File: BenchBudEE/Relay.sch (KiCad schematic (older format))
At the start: 0 parts

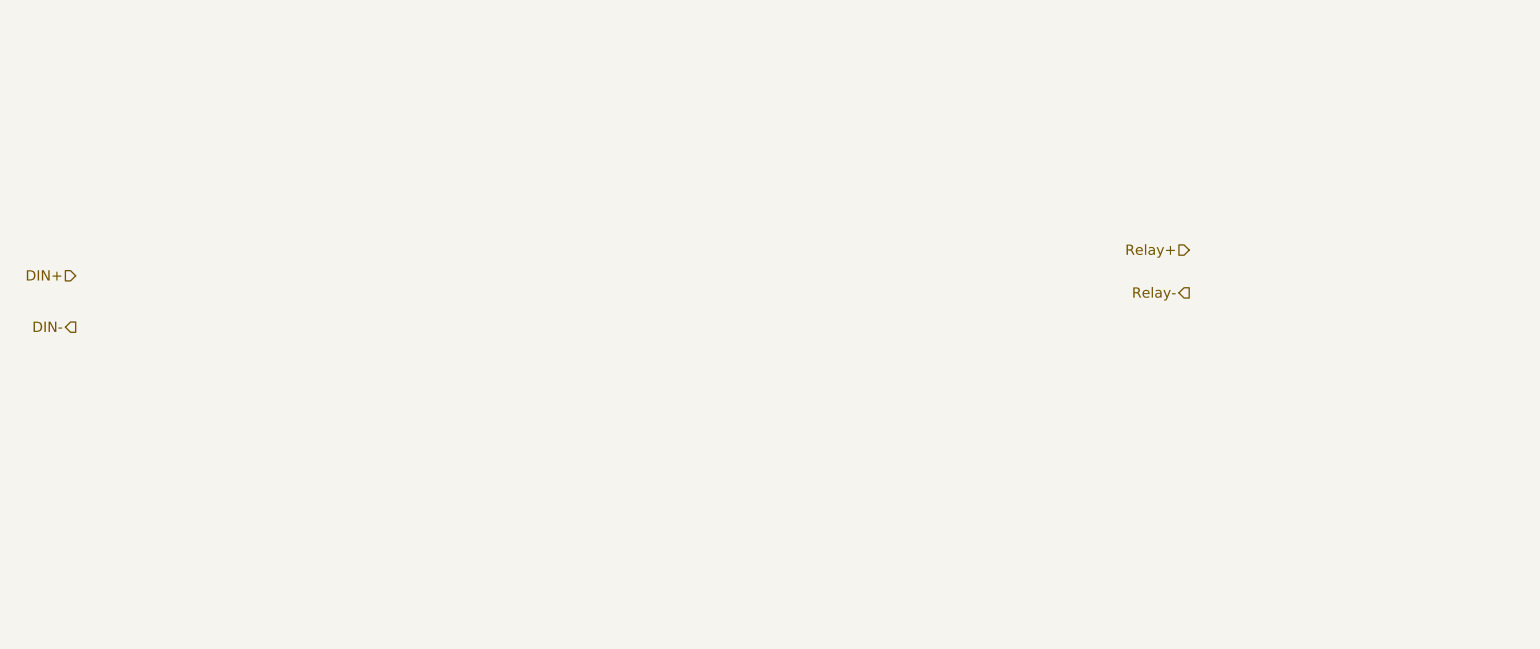
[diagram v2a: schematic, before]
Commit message: Relay block diagram
Relay block diagram and BenchBudEE library created
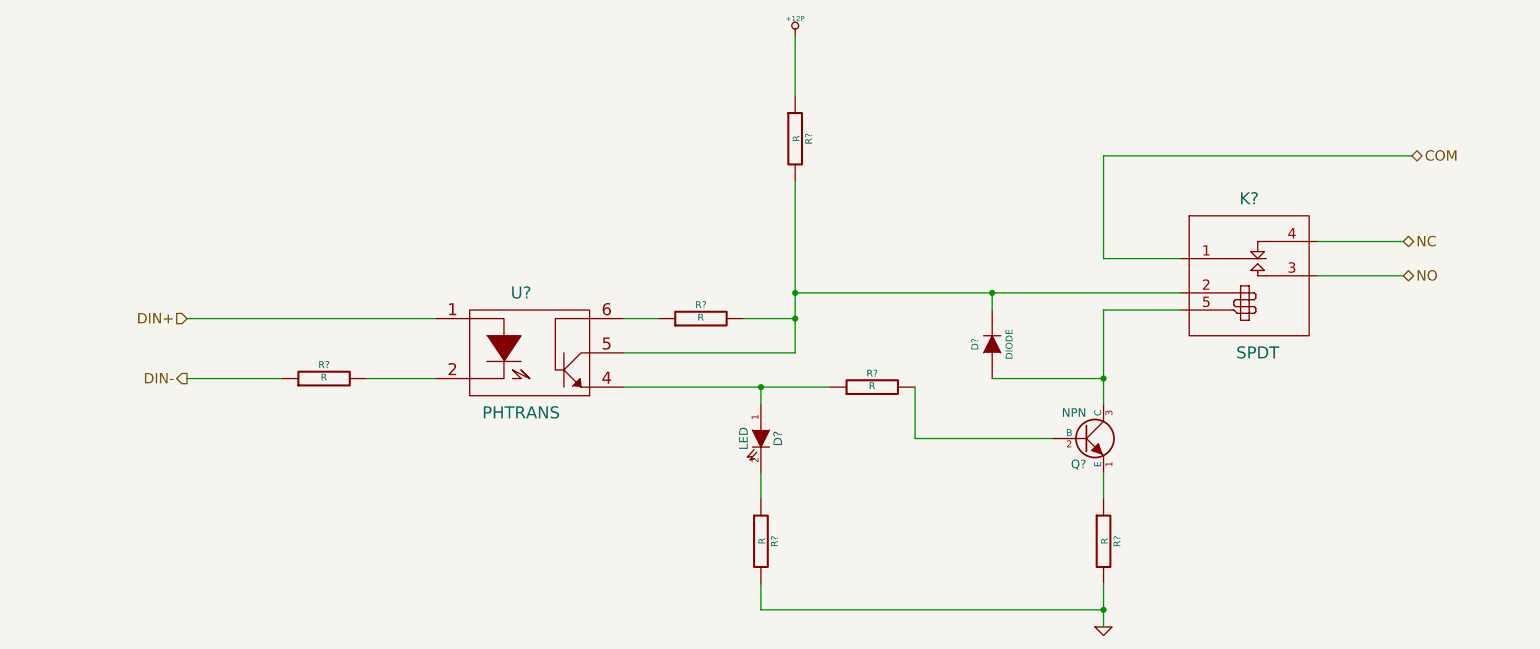
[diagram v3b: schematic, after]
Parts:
- added D?: LED, ~, symbol LED
- added D?: DIODE, ~, symbol DIODE
- added K?: SPDT, ~, symbol SPDT
- added Q?: NPN, ~, symbol NPN
- added R? (x6): R, ~, symbol R
- added U?: PHTRANS, ~, symbol PHTRANS
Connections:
- net DIN+: now also U?.1
- net DIN-: now also R?.1
- new net: R?.2, U?.2
- new net: D?.1 (A), R?.1, U?.4
- new net: D?.2 (K), K?.2 (COIL+), R?.2, R?.2, U?.5
- new net: R?.1, U?.6
- new net: Q?.1 (E), R?.1
- new net: Q?.2 (B), R?.2
- new net: D?.1 (A), K?.5 (COIL-), Q?.3 (C)
- new net: D?.2 (K), R?.1
- new net +12P: R?.1
- new net COM: K?.1 (COM)
- new net GND: R?.2, R?.2
- new net NC: K?.4 (NC)
- new net NO: K?.3 (NO)
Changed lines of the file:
@@
 LIBS:contrib
 LIBS:valves
+LIBS:BenchBuddy
 LIBS:BenchBudEE-cache
 EELAYER 27 0
@@
 Sheet 8 8
 Title ""
-Date "4 feb 2014"
+Date "8 feb 2014"
 Rev ""
 Comp ""
@@
 Comment4 ""
 $EndDescr
-Text HLabel 2300 2750 0    60   Input ~ 0
+Text HLabel 2950 3000 0    60   Input ~ 0
 DIN+
-Text HLabel 2300 3050 0    60   Output ~ 0
+Text HLabel 2950 3350 0    60   Output ~ 0
 DIN-
-Text HLabel 8800 2600 0    60   Input ~ 0
-Relay+
-Text HLabel 8800 2850 0    60   Output ~ 0
-Relay-
+Text HLabel 10050 2550 2    60   BiDi ~ 0
+NC
+Text HLabel 10050 2750 2    60   BiDi ~ 0
+NO
+$Comp
+L PHTRANS U?
+U 1 1 52F62922
+P 4950 3200
+F 0 "U?" H 4900 3550 70  0000 C CNN
+F 1 "PHTRANS" H 4900 2850 70  0000 C CNN
+F 2 "~" H 4950 3200 60  0000 C CNN
+F 3 "~" H 4950 3200 60  0000 C CNN
+	1    4950 3200
+	1    0    0    -1
+$EndComp
+$Comp
+L R R?
+U 1 1 52F62931
+P 8300 4300
+F 0 "R?" V 8380 4300 40  0000 C CNN
+F 1 "R" V 8307 4301 40  0000 C CNN
+F 2 "~" V 8230 4300 30  0000 C CNN
+F 3 "~" H 8300 4300 30  0000 C CNN
+	1    8300 4300
+	1    0    0    -1
+$EndComp
+$Comp
+L NPN Q?
+U 1 1 52F62940
+P 8200 3700
+F 0 "Q?" H 8200 3550 50  0000 R CNN
+F 1 "NPN" H 8200 3850 50  0000 R CNN
+F 2 "~" H 8200 3700 60  0000 C CNN
+F 3 "~" H 8200 3700 60  0000 C CNN
+	1    8200 3700
+	1    0    0    -1
+$EndComp
+$Comp
+L LED D?
+U 1 1 52F6294F
+P 6300 3700
+F 0 "D?" H 6300 3800 50  0000 C CNN
+F 1 "LED" H 6300 3600 50  0000 C CNN
+F 2 "~" H 6300 3700 60  0000 C CNN
+F 3 "~" H 6300 3700 60  0000 C CNN
+	1    6300 3700
+	0    1    1    0
+$EndComp
+$Comp
+L SPDT K?
+U 1 1 52F62EE5
+P 9150 2600
+F 0 "K?" H 9150 2900 70  0000 C CNN
+F 1 "SPDT" H 9200 2000 70  0000 C CNN
+F 2 "~" H 9150 2600 60  0000 C CNN
+F 3 "~" H 9150 2600 60  0000 C CNN
+	1    9150 2600
+	1    0    0    -1
+$EndComp
+Text HLabel 10100 2050 2    60   BiDi ~ 0
+COM
+Wire Wire Line
+	9550 2550 10050 2550
+Wire Wire Line
+	10050 2750 9550 2750
+Wire Wire Line
+	8750 2950 8300 2950
+Wire Wire Line
+	8300 2950 8300 3500
+Wire Wire Line
+	8300 3900 8300 4050
+Wire Wire Line
+	8300 4550 8300 4800
+$Comp
+L GND #PWR?
+U 1 1 52F62F52
+P 8300 4800
+F 0 "#PWR?" H 8300 4800 30  0001 C CNN
+F 1 "GND" H 8300 4730 30  0001 C CNN
+F 2 "" H 8300 4800 60  0000 C CNN
+F 3 "" H 8300 4800 60  0000 C CNN
+	1    8300 4800
+	1    0    0    -1
+$EndComp
+Wire Wire Line
+	6300 3500 6300 3400
+Connection ~ 6300 3400
+$Comp
+L R R?
+U 1 1 52F62F9C
+P 6300 4300
+F 0 "R?" V 6380 4300 40  0000 C CNN
+F 1 "R" V 6307 4301 40  0000 C CNN
+F 2 "~" V 6230 4300 30  0000 C CNN
+F 3 "~" H 6300 4300 30  0000 C CNN
+	1    6300 4300
+	1    0    0    -1
+$EndComp
+Wire Wire Line
+	6300 3900 6300 4050
+Wire Wire Line
+	6300 4550 6300 4700
+Wire Wire Line
+	6300 4700 8300 4700
+Connection ~ 8300 4700
+$Comp
+L R R?
+U 1 1 52F62FC5
+P 6950 3400
+F 0 "R?" V 7030 3400 40  0000 C CNN
+F 1 "R" V 6957 3401 40  0000 C CNN
+F 2 "~" V 6880 3400 30  0000 C CNN
+F 3 "~" H 6950 3400 30  0000 C CNN
+	1    6950 3400
+	0    -1   -1   0
+$EndComp
+Wire Wire Line
+	5500 3400 6700 3400
+$Comp
+L R R?
+U 1 1 52F62FE8
+P 6500 1950
+F 0 "R?" V 6580 1950 40  0000 C CNN
+F 1 "R" V 6507 1951 40  0000 C CNN
+F 2 "~" V 6430 1950 30  0000 C CNN
+F 3 "~" H 6500 1950 30  0000 C CNN
+	1    6500 1950
+	1    0    0    -1
+$EndComp
+Wire Wire Line
+	8750 2850 6500 2850
+Wire Wire Line
+	6500 2200 6500 3200
+Wire Wire Line
+	6500 1700 6500 1350
+$Comp
+L +12P #PWR?
+U 1 1 52F63026
+P 6500 1350
+F 0 "#PWR?" H 6500 1320 30  0001 C CNN
+F 1 "+12P" H 6500 1450 30  0000 C CNN
+F 2 "" H 6500 1350 60  0000 C CNN
+F 3 "" H 6500 1350 60  0000 C CNN
+	1    6500 1350
+	1    0    0    -1
+$EndComp
+$Comp
+L R R?
+U 1 1 52F63033
+P 5950 3000
+F 0 "R?" V 6030 3000 40  0000 C CNN
+F 1 "R" V 5957 3001 40  0000 C CNN
+F 2 "~" V 5880 3000 30  0000 C CNN
+F 3 "~" H 5950 3000 30  0000 C CNN
+	1    5950 3000
+	0    -1   -1   0
+$EndComp
+Wire Wire Line
+	5500 3000 5700 3000
+Wire Wire Line
+	6500 3000 6200 3000
+Connection ~ 6500 2850
+Wire Wire Line
+	6500 3200 5500 3200
+Connection ~ 6500 3000
+$Comp
+L R R?
+U 1 1 52F6308B
+P 3750 3350
+F 0 "R?" V 3830 3350 40  0000 C CNN
+F 1 "R" V 3757 3351 40  0000 C CNN
+F 2 "~" V 3680 3350 30  0000 C CNN
+F 3 "~" H 3750 3350 30  0000 C CNN
+	1    3750 3350
+	0    -1   -1   0
+$EndComp
+Wire Wire Line
+	2950 3000 4400 3000
+Wire Wire Line
+	4400 3350 4000 3350
+Wire Wire Line
+	3500 3350 2950 3350
+Wire Wire Line
+	10100 2050 8300 2050
+Wire Wire Line
+	8300 2050 8300 2650
+Wire Wire Line
+	8300 2650 8750 2650
+Wire Wire Line
+	7200 3400 7200 3700
+Wire Wire Line
+	7200 3700 8000 3700
+$Comp
+L DIODE D?
+U 1 1 52F631F1
+P 7650 3150
+F 0 "D?" H 7650 3250 40  0000 C CNN
+F 1 "DIODE" H 7650 3050 40  0000 C CNN
+F 2 "~" H 7650 3150 60  0000 C CNN
+F 3 "~" H 7650 3150 60  0000 C CNN
+	1    7650 3150
+	0    -1   -1   0
+$EndComp
+Wire Wire Line
+	7650 2950 7650 2850
+Connection ~ 7650 2850
+Wire Wire Line
+	7650 3350 8300 3350
+Connection ~ 8300 3350
 $EndSCHEMATC

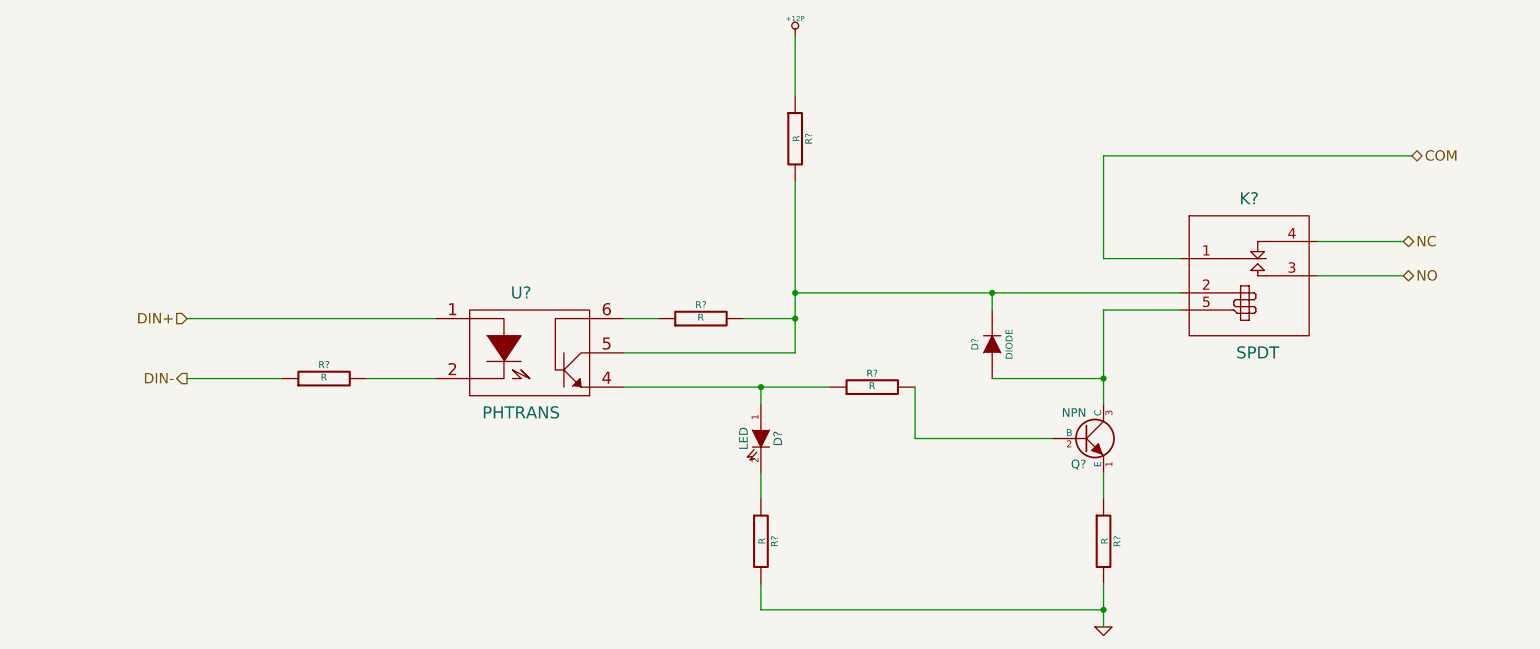
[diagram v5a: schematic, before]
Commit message: Arduino block diagram
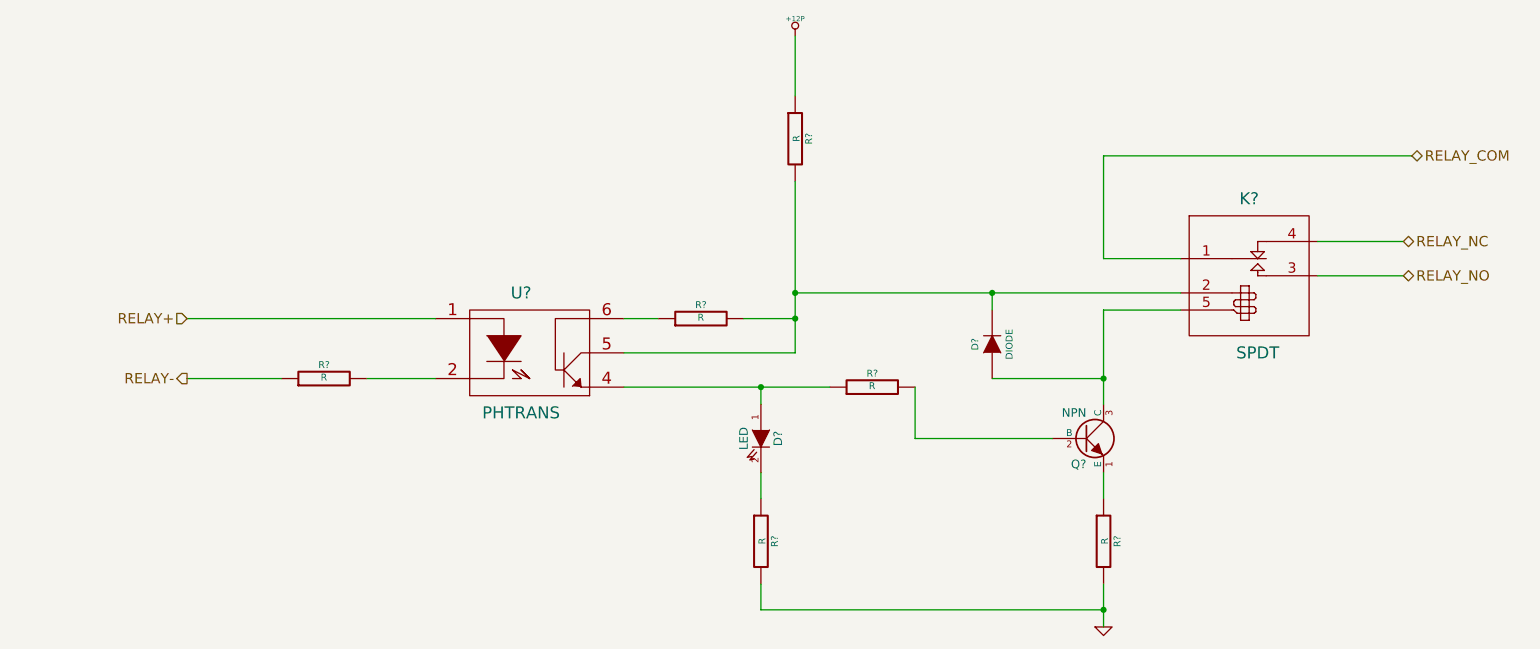
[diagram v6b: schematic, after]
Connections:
- net COM renamed RELAY_COM
- net DIN+ renamed RELAY+
- net DIN- renamed RELAY-
- net NC renamed RELAY_NC
- net NO renamed RELAY_NO
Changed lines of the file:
@@
 $EndDescr
 Text HLabel 2950 3000 0    60   Input ~ 0
-DIN+
+RELAY+
 Text HLabel 2950 3350 0    60   Output ~ 0
-DIN-
+RELAY-
 Text HLabel 10050 2550 2    60   BiDi ~ 0
-NC
+RELAY_NC
 Text HLabel 10050 2750 2    60   BiDi ~ 0
-NO
+RELAY_NO
 $Comp
 L PHTRANS U?
@@
 $EndComp
 Text HLabel 10100 2050 2    60   BiDi ~ 0
-COM
+RELAY_COM
 Wire Wire Line
 	9550 2550 10050 2550
